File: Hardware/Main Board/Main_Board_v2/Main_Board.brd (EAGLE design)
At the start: 138.4 x 103.8 mm, 49 parts, among them IC1 MBED_MICROCONTROLLER, IC2 NE555, Q1 IRF3704, Q2 BS170

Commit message: Main Board Ready for In-House Manufacture
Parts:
- removed POWER_SUPPLY: TRACO_ISOLATED_SUPPLY, ekohub2013:TRACO_ISOLATED_SUPPLY
- added 2N7000: (no value), jumper:JP2
- added U$10, U$11, U$12: (no value), holes:3,0
- added U$4: INPUT_VOLTAGE_CONNECTOR, ekohub2013:INPUT_VOLTAGE_CONNECTOR
- added U$9: TRACO_ISOLATED_SUPPLY, ekohub2013:TRACO_ISOLATED_SUPPLY
- C10: value (none) -> 10n
- DIS1: device display-lcd:TUXGR_16X2_R2 -> display-lcd3:TUXGR_16X2_R2
- JP10: value (none) -> POWER
- R13: value (none) -> 1M
- R4: value (none) -> 300k
- R7: value 60 -> 20
- moved DIS1 34.8 mm to (13.3, 11.4)
- moved C8 34.1 mm to (38.7, 69.8), turned to 270 degrees
- moved C9 33.3 mm to (30.5, 74.9)
- moved R7 25.0 mm to (80.0, 33.0), turned to 270 degrees
- moved R6 8.03 mm to (25.4, 47.0), turned to 180 degrees
- moved C1 1.27 mm to (8.89, 47.0)
- turned D2 to 270 degrees
- turned D3 to 270 degrees
- turned D4 to 270 degrees
- turned D5 to 270 degrees
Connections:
- removed net BACKLIGHT: IC2.3, R7.1
- new net N$7: 2N7000.2, IC2.3
- new net P16_LCD: 2N7000.1, DIS1.16
- net 5V_MBED: now also R7.1
- net GND: now also 2N7000.3, U$9.P$16; no longer DIS1.16, POWER_SUPPLY.P$16
- net VIN: now also U$9.P$14; no longer POWER_SUPPLY.P$14
- net VIN+: now also U$4.V+, U$9.P$22, U$9.P$23; no longer POWER_SUPPLY.P$22, POWER_SUPPLY.P$23
- net VIN-: now also U$4.V-, U$9.P$2, U$9.P$3; no longer POWER_SUPPLY.P$2, POWER_SUPPLY.P$3
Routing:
- net P16_LCD: track 0.00 -> 72.7 mm
- net BACKLIGHT: track 72.4 -> 0.00 mm, vias 1 -> 0
- net VIN-: track 2.54 -> 36.9 mm
- net VIN: track 89.0 -> 54.9 mm
- net N$45: track 7.25 -> 38.2 mm
- net 5V_MBED: track 314.5 -> 332.5 mm
- net VIN+: track 3.17 -> 20.1 mm
- net N$7: track 0.00 -> 14.0 mm
- net N$3: track 3.79 -> 9.12 mm
- net P8: track 65.5 -> 61.5 mm
- net P7: track 56.6 -> 52.6 mm
- net P24: track 38.4 -> 35.1 mm
- net P21: track 56.9 -> 53.6 mm
- net P23: track 43.5 -> 40.9 mm
- net P22: track 50.6 -> 48.0 mm
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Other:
- outline, holes or cut-outs redrawn

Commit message: Added Gerber Files for Main Board
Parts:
- removed Q1: IRF3704, transistor-power:TO220AH
- added Q3: IRF3704L-V, transistor-power:TO262-V
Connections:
- net 5V: now also Q3.3; no longer Q1.E
- net MODEM: now also Q3.2; no longer Q1.C
- net N$5: now also Q3.1; no longer Q1.B
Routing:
- net 5V: track 6.88 -> 9.42 mm
- net MODEM: track 27.7 -> 25.8 mm
- net N$5: track 16.8 -> 17.6 mm
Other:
- outline, holes or cut-outs redrawn
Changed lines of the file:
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@@
 <board>
 <plain>
-<wire x1="1.27" y1="106.35" x2="1.27" y2="5.08" width="0" layer="20"/>
+<wire x1="138.41" y1="107.62" x2="3.27" y2="107.62" width="0" layer="20"/>
+<wire x1="3.27" y1="107.62" x2="1.27" y2="105.62" width="0" layer="20" curve="90"/>
+<wire x1="1.27" y1="105.62" x2="1.27" y2="5.08" width="0" layer="20"/>
 <wire x1="1.27" y1="5.08" x2="2.54" y2="3.81" width="0" layer="20" curve="90"/>
 <wire x1="2.54" y1="3.81" x2="138.41" y2="3.81" width="0" layer="20"/>
@@
 <wire x1="139.68" y1="5.08" x2="139.68" y2="106.35" width="0" layer="20"/>
 <wire x1="139.68" y1="106.35" x2="138.41" y2="107.62" width="0" layer="20" curve="90"/>
-<wire x1="138.41" y1="107.62" x2="2.54" y2="107.62" width="0" layer="20"/>
-<wire x1="2.54" y1="107.62" x2="1.27" y2="106.35" width="0" layer="20" curve="90"/>
 <dimension x1="139.68" y1="3.81" x2="139.68" y2="107.62" x3="149.86" y3="55.715" layer="20"/>
 <dimension x1="1.27" y1="3.81" x2="139.68" y2="3.81" x3="70.475" y3="-3.81" layer="20"/>
@@
 <element name="C2" library="capacitor-wima" package="C5B3" value="100nF" x="21.59" y="104.14" rot="R180"/>
 <element name="C3" library="capacitor-wima" package="C5B3" value="100nF" x="129.54" y="22.86"/>
-<element name="Q1" library="transistor-power" package="TO220AH" value="IRF3704" x="105.41" y="106.68"/>
 <element name="Q2" library="transistor-small-signal" package="SOT54E" value="BS170" x="97.79" y="100.33"/>
 <element name="R13" library="rcl" package="0411/12" value="1M" x="102.87" y="93.98"/>
@@
 <element name="U$11" library="holes" package="3,0" value="" x="133.35" y="83.82"/>
 <element name="U$12" library="holes" package="3,0" value="" x="5.08" y="38.1"/>
+<element name="Q3" library="transistor-power" package="TO262-V" value="IRF3704L-V" x="105.41" y="102.87"/>
 </elements>
 <signals>
@@
 <contactref element="C9" pad="2"/>
 <polygon width="0.4064" layer="1">
-<vertex x="1.27" y="6.35"/>
-<vertex x="1.27" y="106.68" curve="-90"/>
-<vertex x="3.81" y="107.95"/>
-<vertex x="139.7" y="107.95"/>
+<vertex x="137.7" y="3.81"/>
+<vertex x="3.27" y="3.81" curve="-90"/>
+<vertex x="1.27" y="5.81"/>
+<vertex x="1.27" y="105.95" curve="-90"/>
+<vertex x="3.27" y="107.95"/>
+<vertex x="137.7" y="107.95" curve="-90"/>
+<vertex x="139.7" y="105.95"/>
 <vertex x="139.7" y="5.81" curve="-90"/>
-<vertex x="137.7" y="3.81"/>
-<vertex x="3.81" y="3.81" curve="-90"/>
 </polygon>
 <polygon width="0.4064" layer="16">
-<vertex x="138.43" y="105.95"/>
+<vertex x="139.7" y="105.95"/>
 <vertex x="139.715984375" y="5.835609375" curve="-90.736003"/>
 <vertex x="137.716146875" y="3.810040625"/>
 <vertex x="2.54" y="3.81" curve="-90"/>
 <vertex x="1.27" y="5.08"/>
-<vertex x="1.27" y="106.68" curve="-90"/>
-<vertex x="2.54" y="107.95"/>
+<vertex x="1.27" y="105.95" curve="-90"/>
+<vertex x="3.27" y="107.95"/>
 <vertex x="136.43" y="107.95" curve="-90"/>
 </polygon>
@@
 </signal>
 <signal name="N$5">
-<contactref element="Q1" pad="B"/>
 <contactref element="Q2" pad="D"/>
 <contactref element="R13" pad="1"/>
-<wire x1="96.52" y1="93.98" x2="96.52" y2="100.33" width="0.8128" layer="16"/>
-<wire x1="100.33" y1="97.79" x2="102.87" y2="100.33" width="0.8128" layer="16"/>
-<wire x1="100.33" y1="97.79" x2="100.33" y2="95.25" width="0.8128" layer="16"/>
-<wire x1="100.33" y1="95.25" x2="99.06" y2="93.98" width="0.8128" layer="16"/>
-<wire x1="99.06" y1="93.98" x2="96.52" y2="93.98" width="0.8128" layer="16"/>
+<wire x1="96.52" y1="93.98" x2="96.52" y2="99.06" width="0.8128" layer="16"/>
+<contactref element="Q3" pad="1"/>
+<wire x1="96.52" y1="99.06" x2="96.52" y2="100.33" width="0.8128" layer="16"/>
+<wire x1="102.87" y1="102.87" x2="102.87" y2="99.06" width="0.8128" layer="16"/>
+<wire x1="102.87" y1="99.06" x2="101.6" y2="97.79" width="0.8128" layer="16"/>
+<wire x1="101.6" y1="97.79" x2="97.79" y2="97.79" width="0.8128" layer="16"/>
+<wire x1="97.79" y1="97.79" x2="96.52" y2="99.06" width="0.8128" layer="16"/>
 </signal>
 <signal name="5V">
-<contactref element="Q1" pad="E"/>
 <contactref element="R13" pad="2"/>
-<wire x1="109.22" y1="93.98" x2="109.22" y2="99.06" width="0.8128" layer="1"/>
-<wire x1="109.22" y1="99.06" x2="107.95" y2="100.33" width="0.8128" layer="1"/>
+<contactref element="Q3" pad="3"/>
+<wire x1="109.22" y1="93.98" x2="109.22" y2="101.6" width="0.8128" layer="1"/>
+<wire x1="109.22" y1="101.6" x2="107.95" y2="102.87" width="0.8128" layer="1"/>
 </signal>
 <signal name="MODEM">
-<contactref element="Q1" pad="C"/>
 <contactref element="U$1" pad="5V"/>
-<wire x1="105.41" y1="100.33" x2="105.41" y2="97.155" width="0.8128" layer="16"/>
-<wire x1="105.41" y1="97.155" x2="106.045" y2="96.52" width="0.8128" layer="16"/>
-<wire x1="106.045" y1="96.52" x2="113.03" y2="96.52" width="0.8128" layer="16"/>
-<wire x1="113.03" y1="96.52" x2="113.03" y2="100.33" width="0.8128" layer="16"/>
-<wire x1="113.03" y1="100.33" x2="120.65" y2="100.33" width="0.8128" layer="16"/>
-<wire x1="120.65" y1="100.33" x2="121.92" y2="101.6" width="0.8128" layer="16"/>
-<wire x1="121.92" y1="101.6" x2="124.97" y2="101.6" width="0.8128" layer="16"/>
+<wire x1="113.03" y1="101.6" x2="124.97" y2="101.6" width="0.8128" layer="16"/>
 <wire x1="124.97" y1="101.6" x2="125.2" y2="101.37" width="0.8128" layer="16"/>
+<contactref element="Q3" pad="2"/>
+<wire x1="113.03" y1="101.6" x2="109.22" y2="97.79" width="0.8128" layer="16"/>
+<wire x1="109.22" y1="97.79" x2="106.68" y2="97.79" width="0.8128" layer="16"/>
+<wire x1="106.68" y1="97.79" x2="105.41" y2="99.06" width="0.8128" layer="16"/>
+<wire x1="105.41" y1="99.06" x2="105.41" y2="102.87" width="0.8128" layer="16"/>
 </signal>
 <signal name="VIN-">

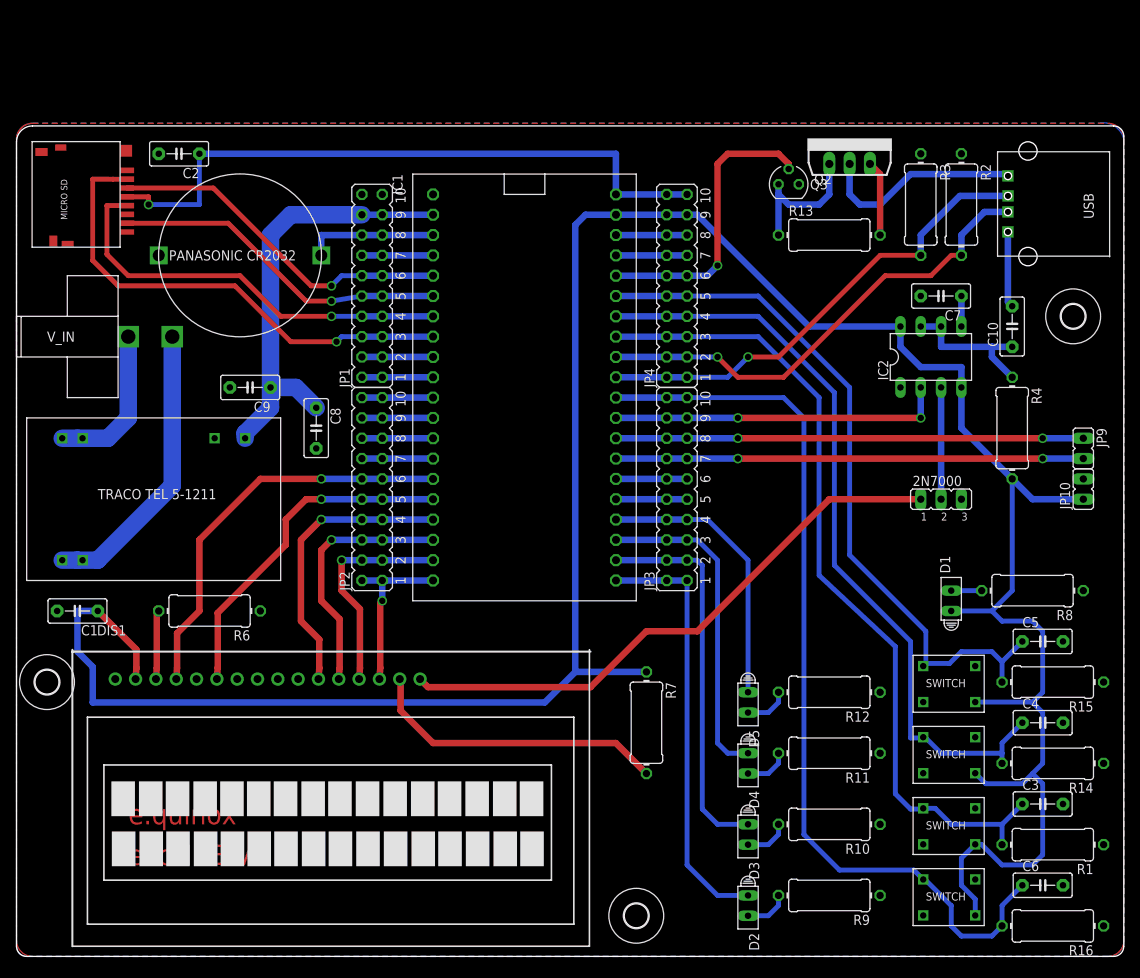
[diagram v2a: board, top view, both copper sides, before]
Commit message: Changed the TRACO Part and USB clearance fix
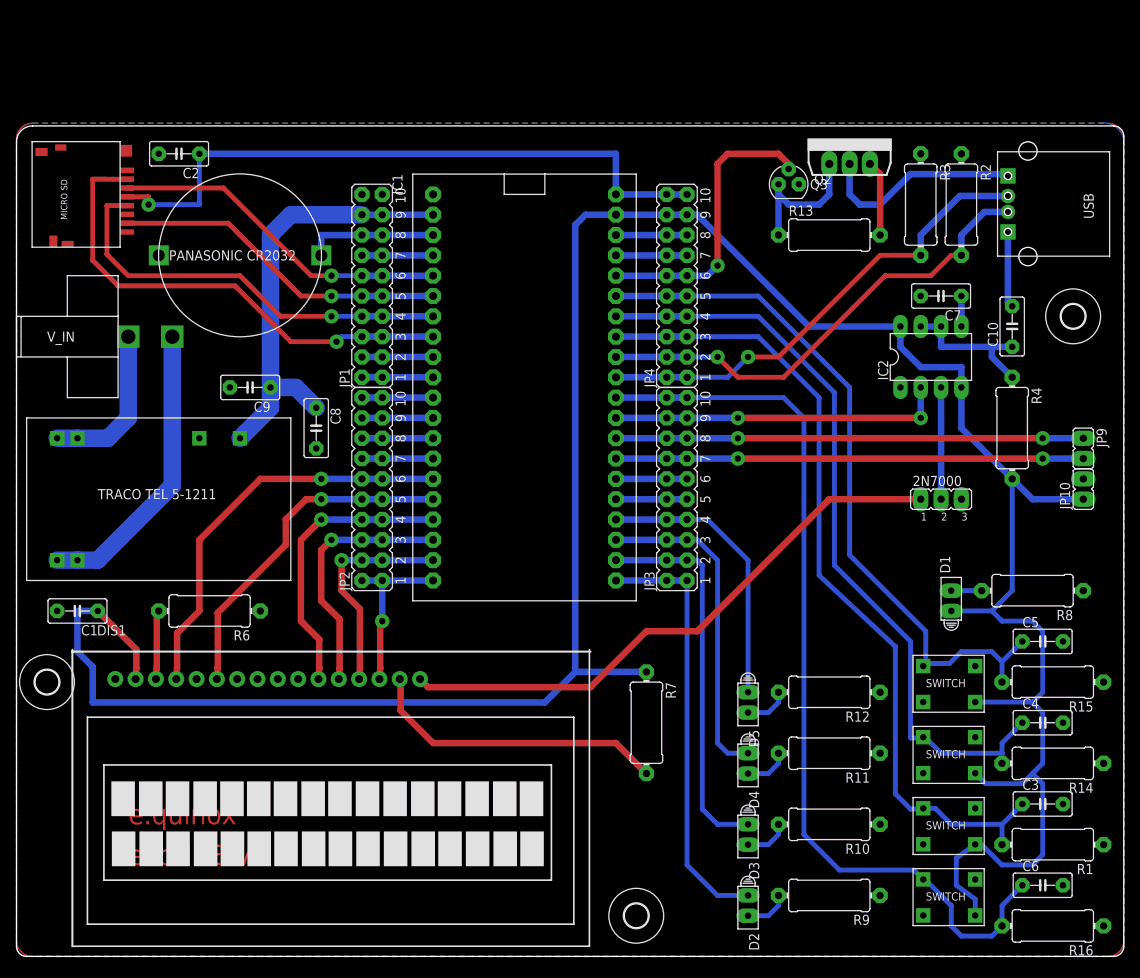
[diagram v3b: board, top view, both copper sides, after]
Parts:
- moved U$1 5.24 mm to (125.7, 96.5)
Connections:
- net D+: now also U$1.D++; no longer U$1.D+
- net D-: now also U$1.D--; no longer U$1.D-
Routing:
- net P5: track 43.8 -> 42.8 mm
- net 5V_MBED: track 332.5 -> 333.5 mm
